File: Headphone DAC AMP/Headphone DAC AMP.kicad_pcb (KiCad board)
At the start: 4 copper layers, 72 parts, among them J1 2137160001, J2 M50-3551042, J4 PINHD_1x2_Male, U2 XU316-1024-QF60B-C24, U6 MCP1727-1802xSN, U7 MCP1727-3302xSN, U8 W25Q16JVSNIQ, U9 TPS717XX, Y1 Crystal_GND24, Y2 LMK6CE049152CDLFR, Y3 ASDLJ-E-45.1584MHz

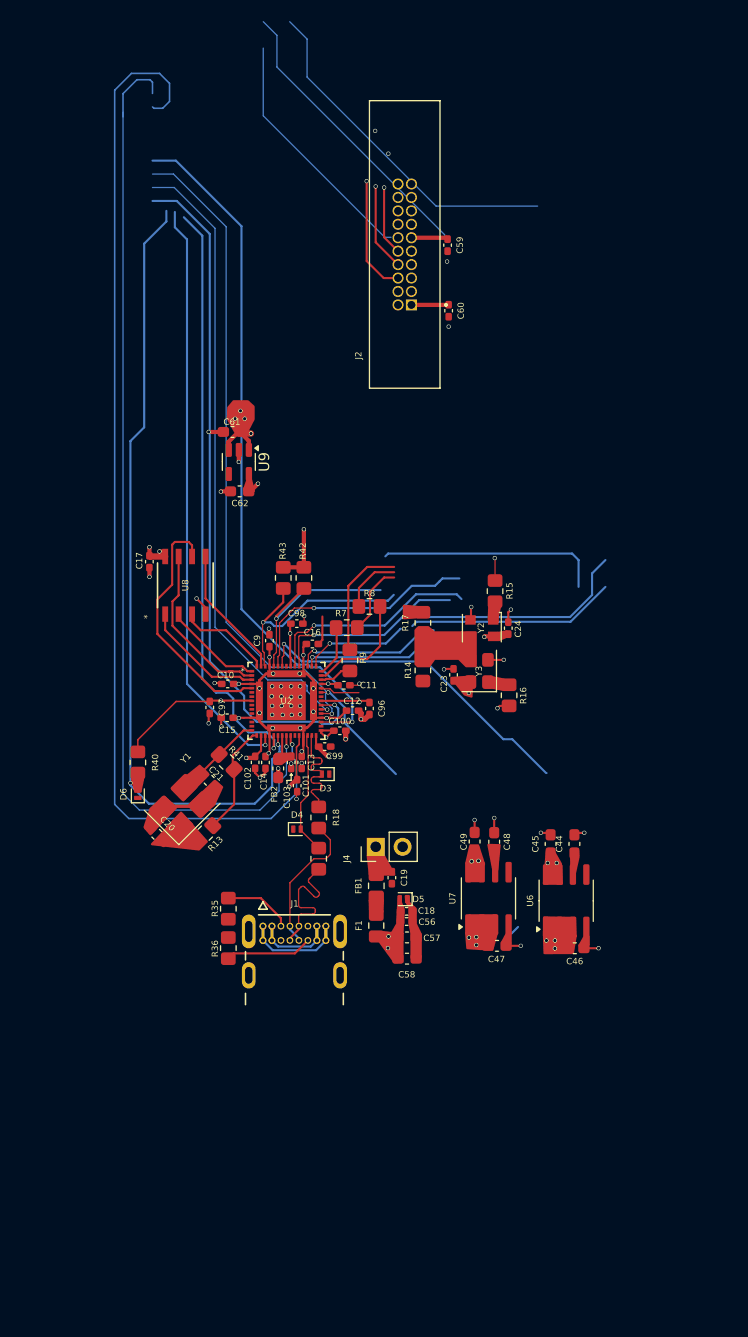
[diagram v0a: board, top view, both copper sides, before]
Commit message: Worked on power schematic
planning to add debugging options
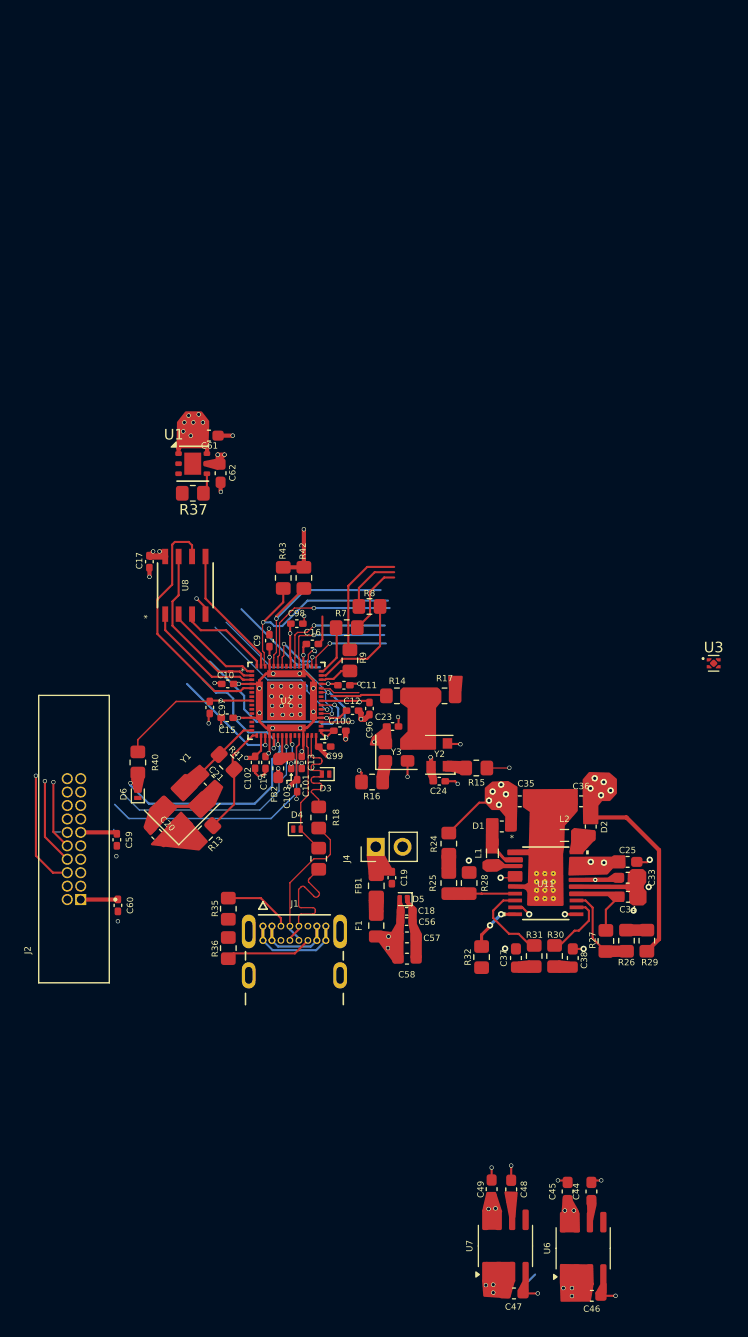
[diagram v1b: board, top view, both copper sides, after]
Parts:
- removed U9: TPS717XX, Package_TO_SOT_SMD:SOT-23-5
- added ?: , , F.Cu at (122.3, 139.1)
- added ?: , , F.Cu at (120.7, 140.7)
- added ?: , , F.Cu at (121.5, 138.3)
- added ?: , , F.Cu at (122.3, 140.7)
- added ?: , , F.Cu at (120.7, 139.1)
- added ?: , , F.Cu at (121.5, 139.1)
- added ?: , , F.Cu at (122.3, 139.9)
- added ?: , , F.Cu at (120.7, 138.3)
- added ?: , , F.Cu at (122.3, 138.3)
- added ?: , , F.Cu at (121.5, 139.9)
- added ?: , , F.Cu at (120.7, 139.9)
- added ?: , , F.Cu at (121.5, 140.7)
- added C25: 10u, Capacitor_SMD:C_0603_1608Metric_Pad1.08x0.95mm_HandSolder, F.Cu at (129.3, 137.2)
- added C33: 1u, Capacitor_SMD:C_0603_1608Metric_Pad1.08x0.95mm_HandSolder, F.Cu at (129.3, 138.7)
- added C34: 1u, Capacitor_SMD:C_0603_1608Metric_Pad1.08x0.95mm_HandSolder, F.Cu at (129.4, 140.5)
- added C35: 10u, Capacitor_SMD:C_0603_1608Metric_Pad1.08x0.95mm_HandSolder, F.Cu at (119.1, 131.5)
- added C36: 10u, Capacitor_SMD:C_0603_1608Metric_Pad1.08x0.95mm_HandSolder, F.Cu at (124.9, 131.5)
- added C37: 47u, Capacitor_SMD:C_0603_1608Metric_Pad1.08x0.95mm_HandSolder, F.Cu at (118.8, 146.3)
- added C38: 47u, Capacitor_SMD:C_0603_1608Metric_Pad1.08x0.95mm_HandSolder, F.Cu at (124.2, 146.3)
- added D1: D_Schottky, Capacitor_SMD:C_0603_1608Metric_Pad1.08x0.95mm_HandSolder, F.Cu at (117.4, 133.8)
- added D2: D_Schottky, Capacitor_SMD:C_0603_1608Metric_Pad1.08x0.95mm_HandSolder, F.Cu at (125.8, 133.9)
- added L1: 3.3u, Inductor_SMD:L_0805_2012Metric, F.Cu at (116.5, 136.4)
- added L2: 4.7u, Inductor_SMD:L_0805_2012Metric, F.Cu at (123.4, 134.7)
- added R24: 560K, Resistor_SMD:R_0805_2012Metric_Pad1.20x1.40mm_HandSolder, F.Cu at (112.4, 135.5)
- added R25: 100K, Resistor_SMD:R_0805_2012Metric_Pad1.20x1.40mm_HandSolder, F.Cu at (114.3, 139.2)
- added R26: 36k, Resistor_SMD:R_0805_2012Metric_Pad1.20x1.40mm_HandSolder, F.Cu at (129.2, 144.7)
- added R27: 100K, Resistor_SMD:R_0805_2012Metric_Pad1.20x1.40mm_HandSolder, F.Cu at (127.3, 144.7)
- added R28: 27K, Resistor_SMD:R_0805_2012Metric_Pad1.20x1.40mm_HandSolder, F.Cu at (112.4, 139.2)
- added R29: 750k, Resistor_SMD:R_0805_2012Metric_Pad1.20x1.40mm_HandSolder, F.Cu at (131.2, 144.7)
- added R30: 4k, Resistor_SMD:R_0805_2012Metric_Pad1.20x1.40mm_HandSolder, F.Cu at (122.4, 146.1)
- added R31: 1k, Resistor_SMD:R_0805_2012Metric_Pad1.20x1.40mm_HandSolder, F.Cu at (120.5, 146.1)
- added R32: DNP, Resistor_SMD:R_0805_2012Metric_Pad1.20x1.40mm_HandSolder, F.Cu at (115.5, 146.2)
- added R37: 100k, Resistor_SMD:R_0805_2012Metric_Pad1.20x1.40mm_HandSolder, F.Cu at (88.2, 102.3)
- added U1: NCV8187AMTW090TAG, Package_SON:WSON-6-1EP_3x3mm_P0.95mm, F.Cu at (88.2, 99.5)
- added U11: ADP5071AREZ-R7, ADP5071:RE-20-1_ADI, F.Cu at (121.6, 139.2)
- added U3: TPS7A20xxxDQN, Package_SON:Texas_X2SON-4_1x1mm_P0.65mm, F.Cu at (137.5, 118.4)
- moved C60 64.3 mm to (81.1, 141.3)
- moved C59 64.3 mm to (81.0, 135.1)
- moved J2 64.3 mm to (77.0, 135.0)
- moved C44 32.9 mm to (125.9, 168.4)
- moved C45 32.9 mm to (123.7, 168.4)
- moved C46 32.9 mm to (125.9, 178.2)
- moved C47 32.9 mm to (118.6, 178.0)
- moved C48 32.9 mm to (118.3, 168.2)
- moved C49 32.9 mm to (116.5, 168.1)
- moved U6 32.9 mm to (125.1, 173.7)
- moved U7 32.9 mm to (117.8, 173.5)
- moved R15 16.8 mm to (115.0, 128.3), turned to 180 degrees
- moved C24 15.9 mm to (111.5, 129.6), turned to 0 degrees
- moved R16 15.3 mm to (105.2, 129.7), turned to 0 degrees
- moved Y2 12.6 mm to (111.5, 127.1), turned to 180 degrees
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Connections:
- C61 pad 1: +1V8 -> +3.3V
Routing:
- net (no net): track 123.4 -> 2.33 mm, vias 0 -> 2
- net /Debug/TCK: track 101.8 -> 24.4 mm
- net /Debug/TMS: track 92.6 -> 21.5 mm
- net /Debug/XMOS_NRST: track 82.4 -> 26.9 mm
- net /Debug/4D0: track 66.3 -> 12.7 mm
- net /Debug/4D3: track 65.4 -> 18.3 mm
- net /Debug/4D1: track 61.8 -> 15.4 mm
- net /Debug/4D2: track 59.9 -> 14.7 mm
- net /Debug/TDI: track 64.0 -> 18.9 mm
- net /Debug/TDO: track 67.8 -> 23.4 mm
- net /Clocking/XTAL1_EN: track 34.3 -> 7.48 mm
- net GND: track 75.0 -> 52.4 mm, vias 46 -> 50
- net /General Power/-5V5: track 0.00 -> 17.8 mm, vias 0 -> 5
- net /USB Audio Input/DAC_GP3: track 14.1 -> 2.07 mm
- net /USB Audio Input/DAC_GP2: track 12.5 -> 0.99 mm
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
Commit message: Added 0.9V regulator footprint
There is still an issue where the nets are not being populated correctly across the schematic to PCB view
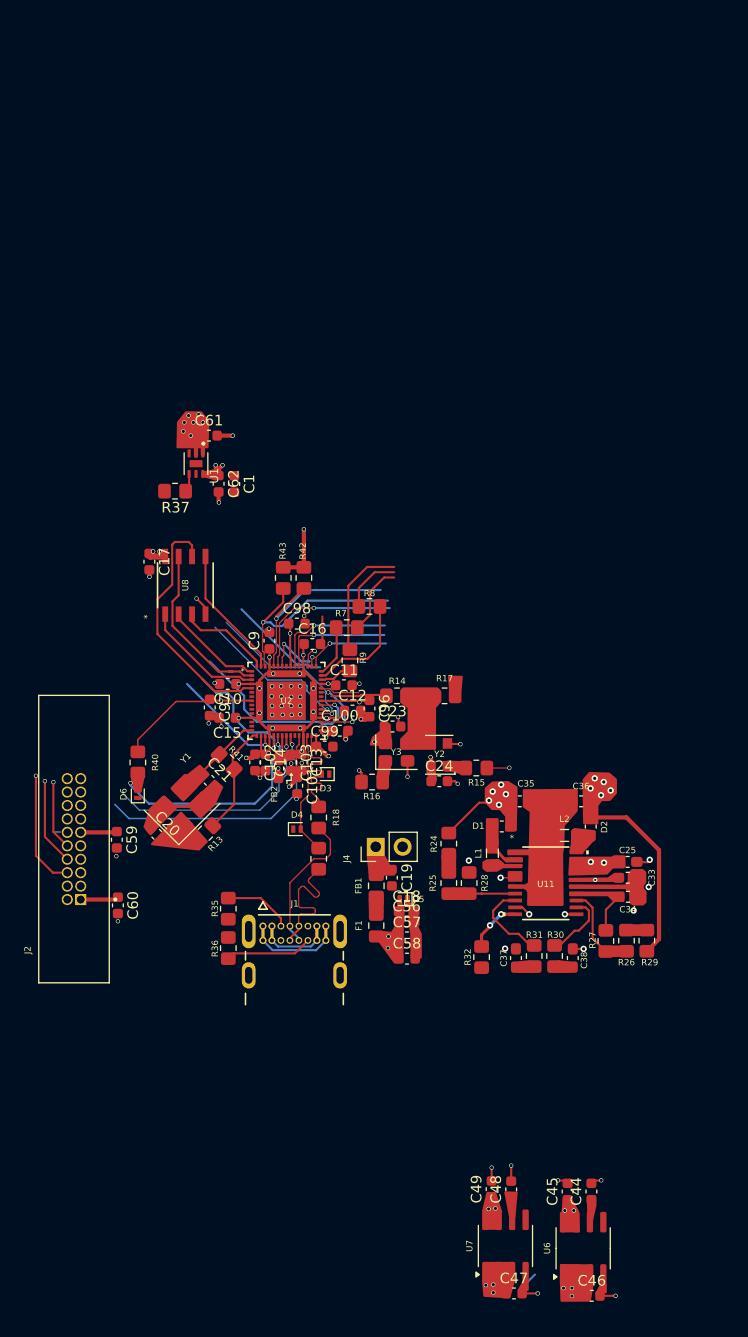
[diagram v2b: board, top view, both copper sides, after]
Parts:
- removed ? (x12): , 
- removed U3: TPS7A20xxxDQN, Package_SON:Texas_X2SON-4_1x1mm_P0.65mm
- added C1: 10u, Capacitor_SMD:C_0603_1608Metric, F.Cu at (92.1, 101.5)
- C10, C100, C101, C102, C103, C11, C12, C13, C14, C15, C16, C17, C18, C19, C23, C24, C56, C59, C60, C9, C96, C97, C98, C99: footprint Capacitor_SMD:C_0402_1005Metric_Pad0.74x0.62mm_HandSolder -> Capacitor_SMD:C_0603_1608Metric
- C20, C21, C44, C45, C46, C47, C48, C49, C57, C58, C61: footprint Capacitor_SMD:C_0603_1608Metric_Pad1.08x0.95mm_HandSolder -> Capacitor_SMD:C_0603_1608Metric
- C62: value 1u -> 10u; footprint Capacitor_SMD:C_0603_1608Metric_Pad1.08x0.95mm_HandSolder -> Capacitor_SMD:C_0603_1608Metric
- U1: footprint Package_SON:WSON-6-1EP_3x3mm_P0.95mm -> NCV8187AMTW090TAG:SON65P200X200X80-7N
- moved R37 1.69 mm to (86.5, 102.2)
- moved C62 1.02 mm to (90.7, 101.4)
- moved U1 0.31 mm to (88.5, 99.5), turned to -90 degrees
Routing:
- net 0V9: track 39.5 -> 38.9 mm

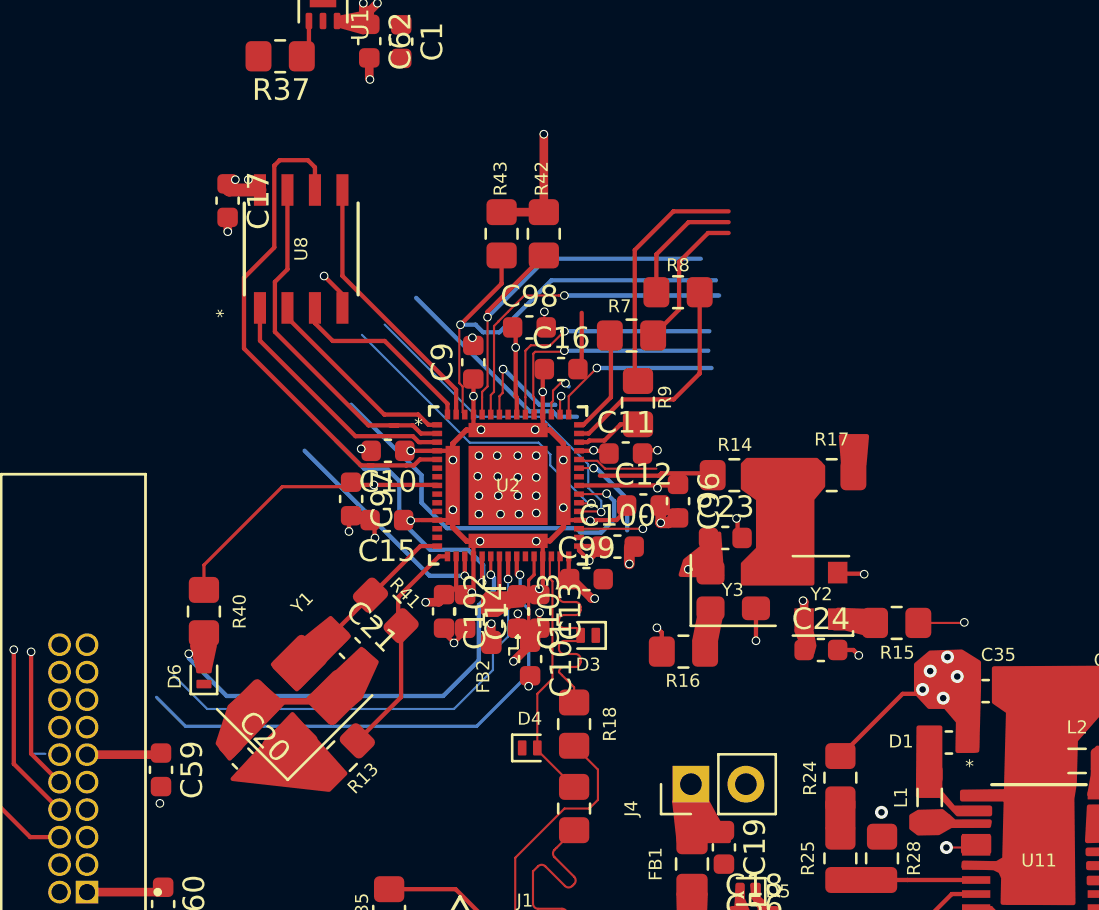
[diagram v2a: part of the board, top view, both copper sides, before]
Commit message: Update PCB layout
Updated component properties and positions in Headphone DAC AMP.kicad_pcb, including changes to reference designators, datasheet fields, and footprint coordinates for several resistors and capacitors.
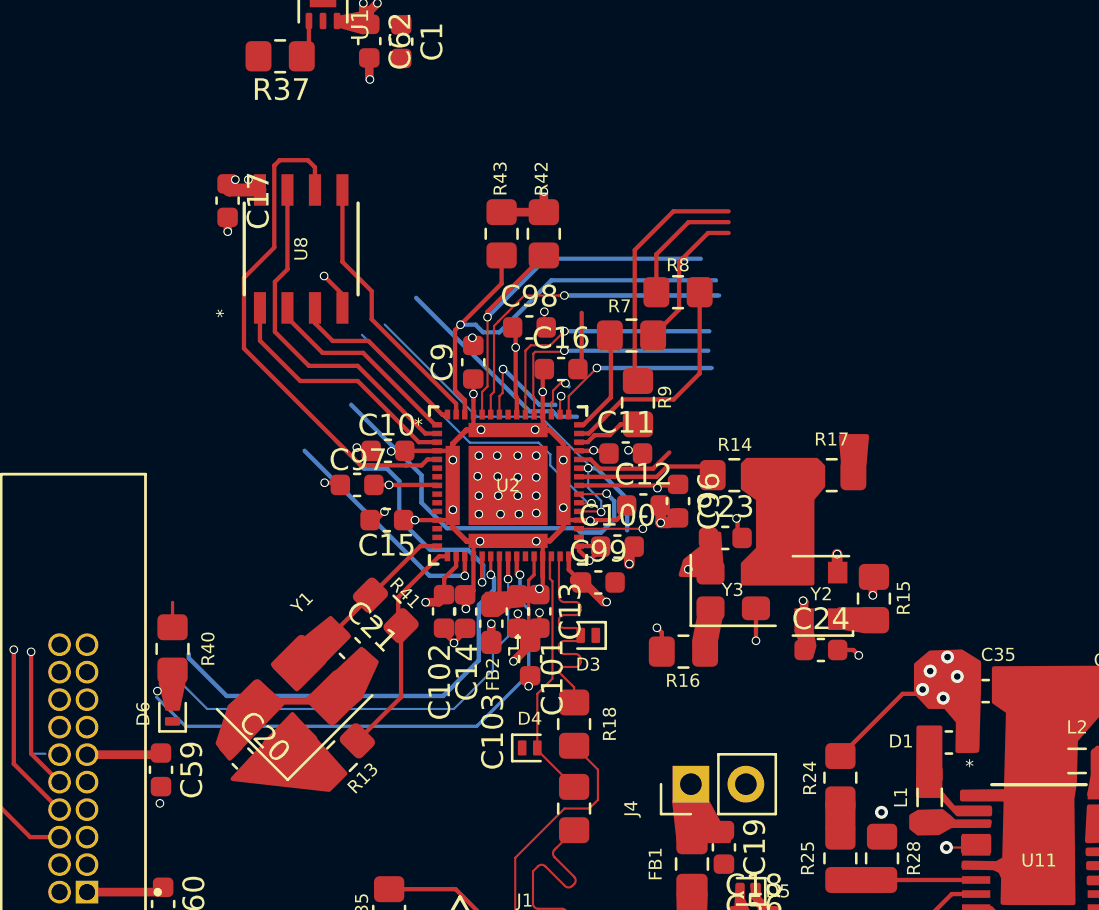
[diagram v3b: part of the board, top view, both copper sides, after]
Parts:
- moved R40 2.25 mm to (81.6, 129.5)
- moved D6 2.25 mm to (81.6, 132.5)
- moved R15 1.54 mm to (114.0, 127.2), turned to -90 degrees
- moved C97 0.71 mm to (90.1, 122.0), turned to 180 degrees
- moved C99 0.57 mm to (101.2, 126.5)
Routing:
- net +1V8: track 46.8 -> 39.1 mm
- net +3.3V: track 48.4 -> 45.7 mm
- net /Clocking/XTAL1_EN: track 7.48 -> 6.14 mm
- net /Clocking/MCLK_XMOS: track 5.89 -> 7.14 mm
- net 0V9: track 38.9 -> 39.8 mm
- net /USB Audio Input/DAC_GP1: track 3.75 -> 4.63 mm
- net /USB Audio Input/QSPI_D3: track 16.9 -> 16.2 mm
- net GND: track 52.4 -> 51.9 mm

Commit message: Worked on layout briefley
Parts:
- removed R24: 560K, Resistor_SMD:R_0805_2012Metric_Pad1.20x1.40mm_HandSolder
- removed R26: 36k, Resistor_SMD:R_0805_2012Metric_Pad1.20x1.40mm_HandSolder
- added C39: 22p, Capacitor_SMD:C_0603_1608Metric_Pad1.08x0.95mm_HandSolder, F.Cu at (119.7, 143.7)
- added C40: 39p, Capacitor_SMD:C_0603_1608Metric_Pad1.08x0.95mm_HandSolder, F.Cu at (123.2, 143.7)
- C37: value 47u -> 330p
- C38: value 47u -> 18n
- L1: value 3.3u -> 0.82u
- L2: value 4.7u -> 10u
- R25: value 100K -> 13K
- R27: value 100K -> 10.7k
- R28: value 27K -> 84.5K
- R29: value 750k -> 90.9k
- R30: value 4k -> 9.09k
- R31: value 1k -> 15k
- moved C46 77.6 mm to (72.7, 121.8), turned to -90 degrees
- moved U6 71.3 mm to (77.2, 121.0), turned to 0 degrees
- moved C47 67.4 mm to (72.7, 128.6), turned to -90 degrees
- moved C45 63.8 mm to (82.5, 119.5), turned to 0 degrees
- moved C44 63.6 mm to (82.5, 121.8), turned to 0 degrees
- moved U7 61.1 mm to (77.2, 127.8), turned to 0 degrees
- moved C49 53.7 mm to (82.6, 126.5), turned to 0 degrees
- moved C48 53.5 mm to (82.5, 128.4), turned to 0 degrees
- moved C59 52.6 mm to (127.9, 111.2)
- moved C60 52.6 mm to (128.0, 117.4)
- moved D6 52.6 mm to (128.4, 108.6)
- moved J2 52.6 mm to (123.9, 111.2)
- moved R40 52.6 mm to (128.4, 105.6)
- moved D3 29.0 mm to (79.3, 148.4)
- moved D4 22.2 mm to (79.3, 146.0)
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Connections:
- net /General Power/-5V5 renamed /General Power/-6V
- C35 pad 2: /General Power/+5V5 -> /General Power/+6V
- D1 pad 1: /General Power/+5V5 -> /General Power/+6V
- R28 pad 1: Net-(R24-Pad2) -> /General Power/+6V
- R29 pad 2: Net-(R26-Pad1) -> Net-(U11-FB2)
- U1 pad 6: +3.3V -> 0V9
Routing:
- net 0V9: track 39.8 -> 59.3 mm
- net /USB Audio Input/PRED+: track 13.9 -> 1.90 mm
- net /USB Audio Input/PRED-: track 13.9 -> 1.98 mm
- net /USB Audio Input/D+: track 11.7 -> 0.10 mm
- net /USB Audio Input/D-: track 11.7 -> 0.20 mm
- net /General Power/+6V: track 0.00 -> 10.5 mm, vias 0 -> 5
- net /General Power/+5V5: track 6.42 -> 0.00 mm, vias 5 -> 0
- net GND: track 51.9 -> 57.3 mm, vias 50 -> 49
- net /General Power/VREF: track 3.68 -> 0.00 mm
- net Net-(U11-FB2): track 6.47 -> 3.20 mm
- net Net-(U11-COMP1): track 8.12 -> 6.09 mm
- net /General Power/-6V: track 17.8 -> 19.4 mm
- net +1V8: track 39.1 -> 37.9 mm
- net +3.3V: track 45.7 -> 44.9 mm
- net Net-(U11-SS): track 5.14 -> 4.42 mm, vias 2 -> 0
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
